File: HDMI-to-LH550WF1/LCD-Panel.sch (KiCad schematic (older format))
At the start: 15 parts

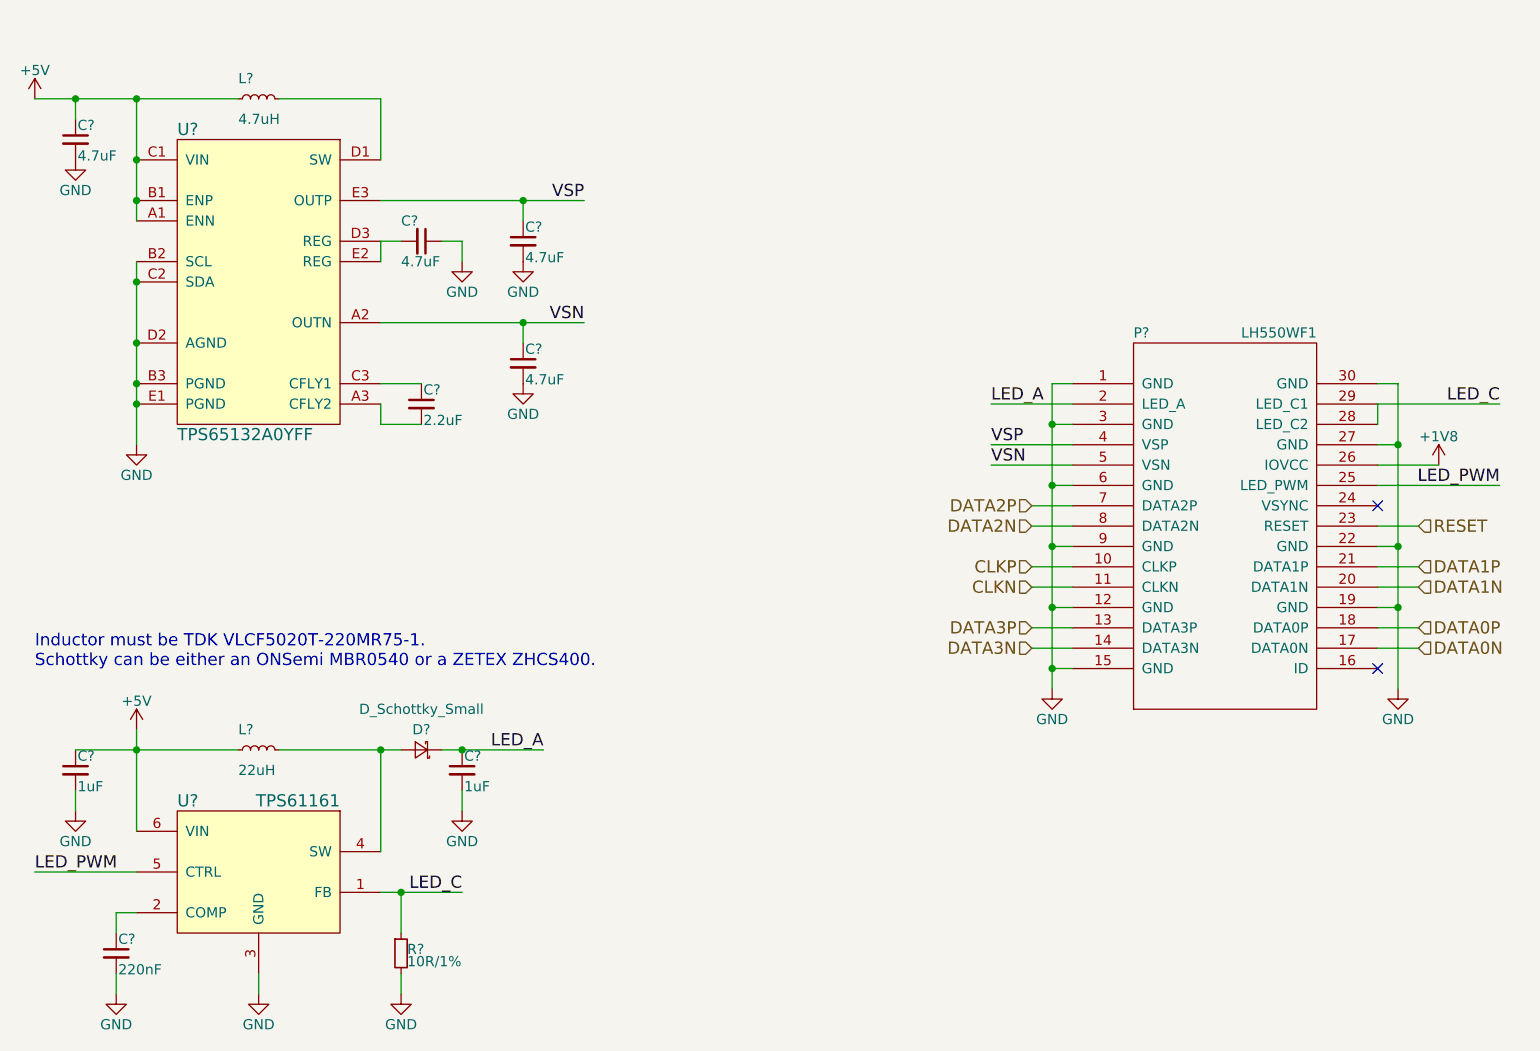
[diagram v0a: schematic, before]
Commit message: Annotated schematic and associated footprints
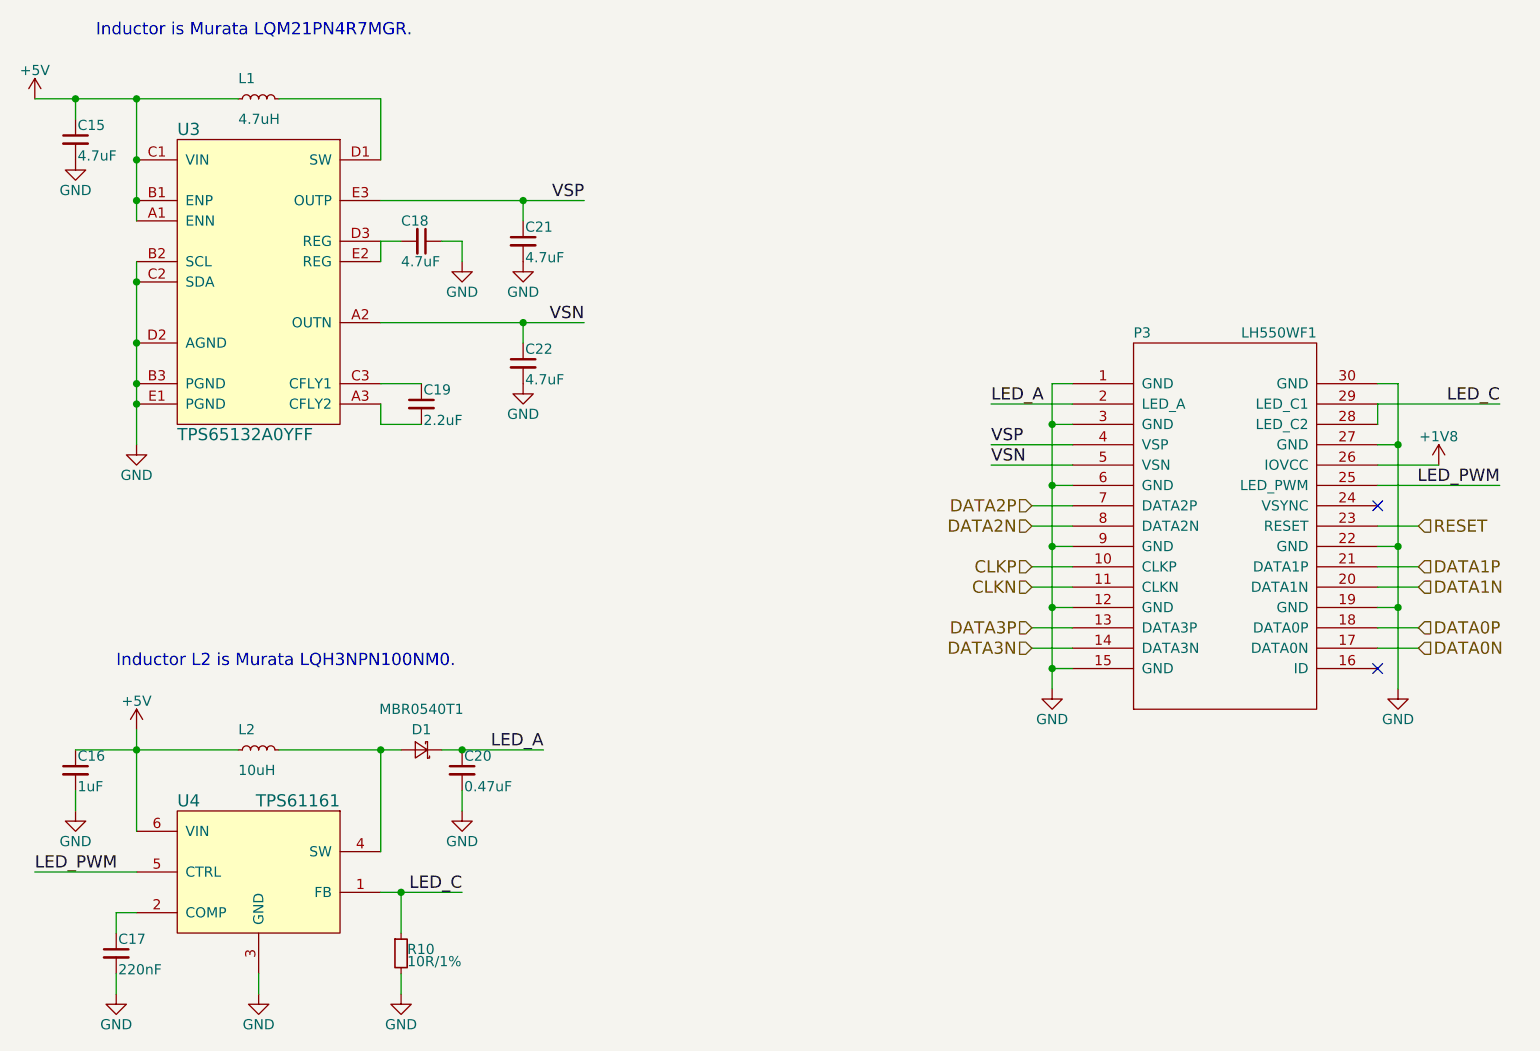
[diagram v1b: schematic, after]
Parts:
- C15, C16, C18, C19, C21, C22: renamed from C?; footprint (none) -> Capacitors_SMD:C_0603
- C17: renamed from C?; footprint (none) -> Capacitors_SMD:C_0402
- C20: renamed from C?; value 1uF -> 0.47uF; footprint (none) -> Capacitors_SMD:C_0603
- D1: renamed from D?; value D_Schottky_Small -> MBR0540T1; footprint (none) -> Diodes_SMD:SOD-123
- L1: renamed from L?; footprint (none) -> Resistors_SMD:R_0805
- L2: renamed from L?; value 22uH -> 10uH; footprint (none) -> Inductors:Inductor_Taiyo-Yuden_MD-3030
- P3: renamed from P?; footprint GB042-30S -> connectors:GB042-30S
- R10: renamed from R?; footprint (none) -> Resistors_SMD:R_0402
- U3: renamed from U?; footprint (none) -> miscellaneous:DSBGA-15_1.5x2.1mm_Pitch0.4mm
- U4: renamed from U?; footprint (none) -> miscellaneous:WSON-6_2x2mm_Pitch0.65mm
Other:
- note added: "Inductor L2 is Murata LQH3NPN100NM0."
- note added: "Inductor is Murata LQM21PN4R7MGR."
- note removed: "Inductor must be TDK VLCF5020T-220MR75-1.\nSchottky can be either an ONSemi MBR0540 or a ZETEX ZHCS400."
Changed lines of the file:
@@
 $EndDescr
 $Comp
-L LH550WF1 P?
+L LH550WF1 P3
 U 1 1 583923EB
 P 7950 3500
-F 0 "P?" H 7500 4450 50  0000 L CNN
+F 0 "P3" H 7500 4450 50  0000 L CNN
 F 1 "LH550WF1" H 8400 4450 50  0000 R CNN
-F 2 "GB042-30S" H 7500 2550 50  0001 L CNN
+F 2 "connectors:GB042-30S" H 7500 2550 50  0001 L CNN
 F 3 "" H 7800 2450 50  0001 C CNN
 	1    7950 3500
@@
 RESET
 $Comp
-L GND #PWR020
+L GND #PWR028
 U 1 1 58392710
 P 8800 4300
-F 0 "#PWR020" H 8800 4050 50  0001 C CNN
+F 0 "#PWR028" H 8800 4050 50  0001 C CNN
 F 1 "GND" H 8800 4150 50  0000 C CNN
 F 2 "" H 8800 4300 50  0000 C CNN
@@
 $EndComp
 $Comp
-L GND #PWR021
+L GND #PWR029
 U 1 1 58392726
 P 7100 4300
-F 0 "#PWR021" H 7100 4050 50  0001 C CNN
+F 0 "#PWR029" H 7100 4050 50  0001 C CNN
 F 1 "GND" H 7100 4150 50  0000 C CNN
 F 2 "" H 7100 4300 50  0000 C CNN
@@
 NoConn ~ 8700 4200
 $Comp
-L +1V8 #PWR022
+L +1V8 #PWR030
 U 1 1 58393DDA
 P 9000 3200
-F 0 "#PWR022" H 9000 3050 50  0001 C CNN
+F 0 "#PWR030" H 9000 3050 50  0001 C CNN
 F 1 "+1V8" H 9000 3340 50  0000 C CNN
 F 2 "" H 9000 3200 50  0000 C CNN
@@
 VSN
 $Comp
-L TPS65132xxYFF U?
+L TPS65132xxYFF U3
 U 1 1 583941C9
 P 3200 2300
-F 0 "U?" H 2800 3050 60  0000 L CNN
+F 0 "U3" H 2800 3050 60  0000 L CNN
 F 1 "TPS65132A0YFF" H 2800 1550 60  0000 L CNN
-F 2 "" H 3100 2700 60  0001 C CNN
+F 2 "miscellaneous:DSBGA-15_1.5x2.1mm_Pitch0.4mm" H 3100 2700 60  0001 C CNN
 F 3 "" H 3100 2700 60  0001 C CNN
 	1    3200 2300
@@
 $EndComp
 $Comp
-L TPS6116x U?
+L TPS6116x U4
 U 1 1 583944F1
 P 3200 5200
-F 0 "U?" H 2800 5550 60  0000 L CNN
+F 0 "U4" H 2800 5550 60  0000 L CNN
 F 1 "TPS61161" H 3600 5550 60  0000 R CNN
-F 2 "" H 3100 5200 60  0001 C CNN
+F 2 "miscellaneous:WSON-6_2x2mm_Pitch0.65mm" H 3100 5200 60  0001 C CNN
 F 3 "" H 3100 5200 60  0001 C CNN
 	1    3200 5200
@@
 LED_PWM
 $Comp
-L +5V #PWR023
+L +5V #PWR031
 U 1 1 58394FDE
 P 2600 4500
-F 0 "#PWR023" H 2600 4350 50  0001 C CNN
+F 0 "#PWR031" H 2600 4350 50  0001 C CNN
 F 1 "+5V" H 2600 4640 50  0000 C CNN
 F 2 "" H 2600 4500 50  0000 C CNN
@@
 $EndComp
 $Comp
-L C_Small C?
+L C_Small C16
 U 1 1 58395057
 P 2300 4700
-F 0 "C?" H 2310 4770 50  0000 L CNN
+F 0 "C16" H 2310 4770 50  0000 L CNN
 F 1 "1uF" H 2310 4620 50  0000 L CNN
-F 2 "" H 2300 4700 50  0000 C CNN
+F 2 "Capacitors_SMD:C_0603" H 2300 4700 50  0001 C CNN
 F 3 "" H 2300 4700 50  0000 C CNN
 	1    2300 4700
@@
 $EndComp
 $Comp
-L L_Small L?
+L L_Small L2
 U 1 1 58395114
 P 3200 4600
-F 0 "L?" V 3300 4700 50  0000 R CNN
-F 1 "22uH" V 3100 4700 50  0000 R CNN
-F 2 "" H 3200 4600 50  0000 C CNN
+F 0 "L2" V 3300 4700 50  0000 R CNN
+F 1 "10uH" V 3100 4700 50  0000 R CNN
+F 2 "Inductors:Inductor_Taiyo-Yuden_MD-3030" H 3200 4600 50  0001 C CNN
 F 3 "" H 3200 4600 50  0000 C CNN
 	1    3200 4600
@@
 $EndComp
 $Comp
-L GND #PWR024
+L GND #PWR032
 U 1 1 58395360
 P 2300 4900
-F 0 "#PWR024" H 2300 4650 50  0001 C CNN
+F 0 "#PWR032" H 2300 4650 50  0001 C CNN
 F 1 "GND" H 2300 4750 50  0000 C CNN
 F 2 "" H 2300 4900 50  0000 C CNN
@@
 $EndComp
 $Comp
-L C_Small C?
+L C_Small C17
 U 1 1 583959D0
 P 2500 5600
-F 0 "C?" H 2510 5670 50  0000 L CNN
+F 0 "C17" H 2510 5670 50  0000 L CNN
 F 1 "220nF" H 2510 5520 50  0000 L CNN
-F 2 "" H 2500 5600 50  0000 C CNN
+F 2 "Capacitors_SMD:C_0402" H 2500 5600 50  0001 C CNN
 F 3 "" H 2500 5600 50  0000 C CNN
 	1    2500 5600
@@
 $EndComp
 $Comp
-L GND #PWR025
+L GND #PWR033
 U 1 1 58395A08
 P 2500 5800
-F 0 "#PWR025" H 2500 5550 50  0001 C CNN
+F 0 "#PWR033" H 2500 5550 50  0001 C CNN
 F 1 "GND" H 2500 5650 50  0000 C CNN
 F 2 "" H 2500 5800 50  0000 C CNN
@@
 $EndComp
 $Comp
-L GND #PWR026
+L GND #PWR034
 U 1 1 58395A97
 P 3200 5800
-F 0 "#PWR026" H 3200 5550 50  0001 C CNN
+F 0 "#PWR034" H 3200 5550 50  0001 C CNN
 F 1 "GND" H 3200 5650 50  0000 C CNN
 F 2 "" H 3200 5800 50  0000 C CNN
@@
 $EndComp
 $Comp
-L GND #PWR027
+L GND #PWR035
 U 1 1 58395AB4
 P 3900 5800
-F 0 "#PWR027" H 3900 5550 50  0001 C CNN
+F 0 "#PWR035" H 3900 5550 50  0001 C CNN
 F 1 "GND" H 3900 5650 50  0000 C CNN
 F 2 "" H 3900 5800 50  0000 C CNN
@@
 $EndComp
 $Comp
-L C_Small C?
+L C_Small C20
 U 1 1 58395AE8
 P 4200 4700
-F 0 "C?" H 4210 4770 50  0000 L CNN
-F 1 "1uF" H 4210 4620 50  0000 L CNN
-F 2 "" H 4200 4700 50  0000 C CNN
+F 0 "C20" H 4210 4770 50  0000 L CNN
+F 1 "0.47uF" H 4210 4620 50  0000 L CNN
+F 2 "Capacitors_SMD:C_0603" H 4200 4700 50  0001 C CNN
 F 3 "" H 4200 4700 50  0000 C CNN
 	1    4200 4700
@@
 Connection ~ 3800 4600
 $Comp
-L D_Schottky_Small D?
+L D_Schottky_Small D1
 U 1 1 583961F5
 P 4000 4600
-F 0 "D?" H 4000 4500 50  0000 C CNN
-F 1 "D_Schottky_Small" H 4000 4400 50  0000 C CNN
-F 2 "" V 4000 4600 50  0000 C CNN
+F 0 "D1" H 4000 4500 50  0000 C CNN
+F 1 "MBR0540T1" H 4000 4400 50  0000 C CNN
+F 2 "Diodes_SMD:SOD-123" V 4000 4600 50  0001 C CNN
 F 3 "" V 4000 4600 50  0000 C CNN
 	1    4000 4600
@@
 	4100 4600 4600 4600
 $Comp
-L GND #PWR028
+L GND #PWR036
 U 1 1 583963D4
 P 4200 4900
-F 0 "#PWR028" H 4200 4650 50  0001 C CNN
+F 0 "#PWR036" H 4200 4650 50  0001 C CNN
 F 1 "GND" H 4200 4750 50  0000 C CNN
 F 2 "" H 4200 4900 50  0000 C CNN
@@
 	4200 4900 4200 4800
 $Comp
-L R_Small R?
+L R_Small R10
 U 1 1 58396477
 P 3900 5600
-F 0 "R?" H 3930 5620 50  0000 L CNN
+F 0 "R10" H 3930 5620 50  0000 L CNN
 F 1 "10R/1%" H 3930 5560 50  0000 L CNN
-F 2 "" H 3900 5600 50  0000 C CNN
+F 2 "Resistors_SMD:R_0402" H 3900 5600 50  0001 C CNN
 F 3 "" H 3900 5600 50  0000 C CNN
 	1    3900 5600
@@
 Connection ~ 4200 4600
 Connection ~ 3900 5300
-Text Notes 2100 4200 0    60   ~ 0
-Inductor must be TDK VLCF5020T-220MR75-1.\nSchottky can be either an ONSemi MBR0540 or a ZETEX ZHCS400.
-$Comp
-L +5V #PWR029
+Text Notes 2500 4200 0    60   ~ 0
+Inductor L2 is Murata LQH3NPN100NM0.
+$Comp
+L +5V #PWR037
 U 1 1 58397D18
 P 2100 1400
-F 0 "#PWR029" H 2100 1250 50  0001 C CNN
+F 0 "#PWR037" H 2100 1250 50  0001 C CNN
 F 1 "+5V" H 2100 1540 50  0000 C CNN
 F 2 "" H 2100 1400 50  0000 C CNN
@@
 $EndComp
 $Comp
-L L_Small L?
+L L_Small L1
 U 1 1 58397E29
 P 3200 1400
-F 0 "L?" V 3300 1500 50  0000 R CNN
+F 0 "L1" V 3300 1500 50  0000 R CNN
 F 1 "4.7uH" V 3100 1500 50  0000 R CNN
-F 2 "" H 3200 1400 50  0000 C CNN
+F 2 "Resistors_SMD:R_0805" H 3200 1400 50  0001 C CNN
 F 3 "" H 3200 1400 50  0000 C CNN
 	1    3200 1400
@@
 	2100 1400 3100 1400
 $Comp
-L C_Small C?
+L C_Small C15
 U 1 1 58398042
 P 2300 1600
-F 0 "C?" H 2310 1670 50  0000 L CNN
+F 0 "C15" H 2310 1670 50  0000 L CNN
 F 1 "4.7uF" H 2310 1520 50  0000 L CNN
-F 2 "" H 2300 1600 50  0000 C CNN
+F 2 "Capacitors_SMD:C_0603" H 2300 1600 50  0001 C CNN
 F 3 "" H 2300 1600 50  0000 C CNN
 	1    2300 1600
@@
 Connection ~ 2300 1400
 $Comp
-L GND #PWR030
+L GND #PWR038
 U 1 1 583981F9
 P 2300 1700
-F 0 "#PWR030" H 2300 1450 50  0001 C CNN
+F 0 "#PWR038" H 2300 1450 50  0001 C CNN
 F 1 "GND" H 2300 1550 50  0000 C CNN
 F 2 "" H 2300 1700 50  0000 C CNN
@@
 Connection ~ 2600 2900
 $Comp
-L GND #PWR031
+L GND #PWR039
 U 1 1 583983E8
 P 2600 3100
-F 0 "#PWR031" H 2600 2850 50  0001 C CNN
+F 0 "#PWR039" H 2600 2850 50  0001 C CNN
 F 1 "GND" H 2600 2950 50  0000 C CNN
 F 2 "" H 2600 3100 50  0000 C CNN
@@
 	3800 3000 3800 2900
 $Comp
-L C_Small C?
+L C_Small C19
 U 1 1 583986B8
 P 4000 2900
-F 0 "C?" H 4010 2970 50  0000 L CNN
+F 0 "C19" H 4010 2970 50  0000 L CNN
 F 1 "2.2uF" H 4010 2820 50  0000 L CNN
-F 2 "" H 4000 2900 50  0000 C CNN
+F 2 "Capacitors_SMD:C_0603" H 4000 2900 50  0001 C CNN
 F 3 "" H 4000 2900 50  0000 C CNN
 	1    4000 2900
@@
 	3800 2200 3800 2100
 $Comp
-L C_Small C?
+L C_Small C18
 U 1 1 58398AB8
 P 4000 2100
-F 0 "C?" V 3900 2000 50  0000 L CNN
+F 0 "C18" V 3900 2000 50  0000 L CNN
 F 1 "4.7uF" V 4100 2000 50  0000 L CNN
-F 2 "" H 4000 2100 50  0000 C CNN
+F 2 "Capacitors_SMD:C_0603" H 4000 2100 50  0001 C CNN
 F 3 "" H 4000 2100 50  0000 C CNN
 	1    4000 2100
@@
 	4200 2100 4200 2200
 $Comp
-L GND #PWR032
+L GND #PWR040
 U 1 1 58398C7D
 P 4200 2200
-F 0 "#PWR032" H 4200 1950 50  0001 C CNN
+F 0 "#PWR040" H 4200 1950 50  0001 C CNN
 F 1 "GND" H 4200 2050 50  0000 C CNN
 F 2 "" H 4200 2200 50  0000 C CNN
@@
 $EndComp
 $Comp
-L C_Small C?
+L C_Small C21
 U 1 1 58398CAF
 P 4500 2100
-F 0 "C?" H 4510 2170 50  0000 L CNN
+F 0 "C21" H 4510 2170 50  0000 L CNN
 F 1 "4.7uF" H 4510 2020 50  0000 L CNN
-F 2 "" H 4500 2100 50  0000 C CNN
+F 2 "Capacitors_SMD:C_0603" H 4500 2100 50  0001 C CNN
 F 3 "" H 4500 2100 50  0000 C CNN
 	1    4500 2100
@@
 Connection ~ 4500 1900
 $Comp
-L GND #PWR033
+L GND #PWR041
 U 1 1 58398F9F
 P 4500 2200
-F 0 "#PWR033" H 4500 1950 50  0001 C CNN
+F 0 "#PWR041" H 4500 1950 50  0001 C CNN
 F 1 "GND" H 4500 2050 50  0000 C CNN
 F 2 "" H 4500 2200 50  0000 C CNN
@@
 $EndComp
 $Comp
-L C_Small C?
+L C_Small C22
 U 1 1 58398FD4
 P 4500 2700
-F 0 "C?" H 4510 2770 50  0000 L CNN
+F 0 "C22" H 4510 2770 50  0000 L CNN
 F 1 "4.7uF" H 4510 2620 50  0000 L CNN
-F 2 "" H 4500 2700 50  0000 C CNN
+F 2 "Capacitors_SMD:C_0603" H 4500 2700 50  0001 C CNN
 F 3 "" H 4500 2700 50  0000 C CNN
 	1    4500 2700
@@
 $EndComp
 $Comp
-L GND #PWR034
+L GND #PWR042
 U 1 1 58399019
 P 4500 2800
-F 0 "#PWR034" H 4500 2550 50  0001 C CNN
+F 0 "#PWR042" H 4500 2550 50  0001 C CNN
 F 1 "GND" H 4500 2650 50  0000 C CNN
 F 2 "" H 4500 2800 50  0000 C CNN
@@
 Connection ~ 2600 2600
 Connection ~ 2600 2300
+Text Notes 2400 1100 0    60   ~ 0
+Inductor is Murata LQM21PN4R7MGR.
 $EndSCHEMATC

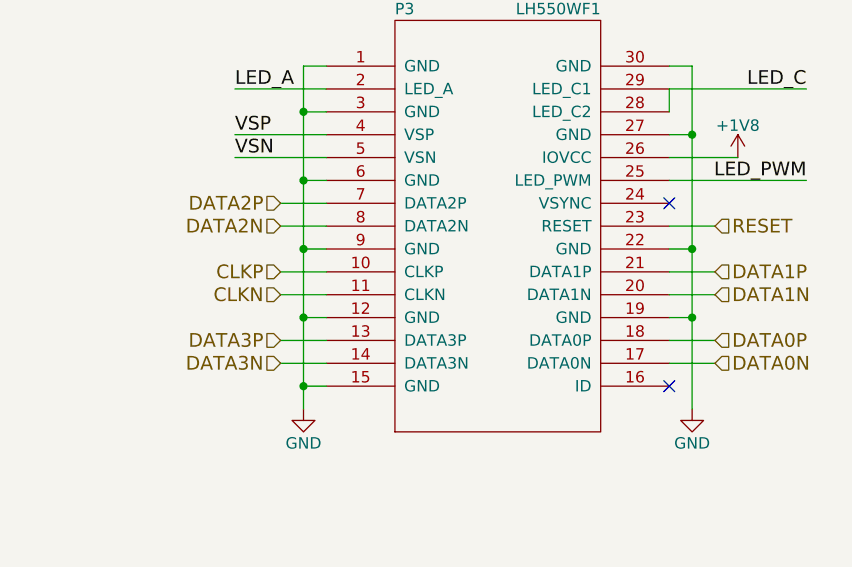
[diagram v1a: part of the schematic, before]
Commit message: Renamed some nets to enable differential routing
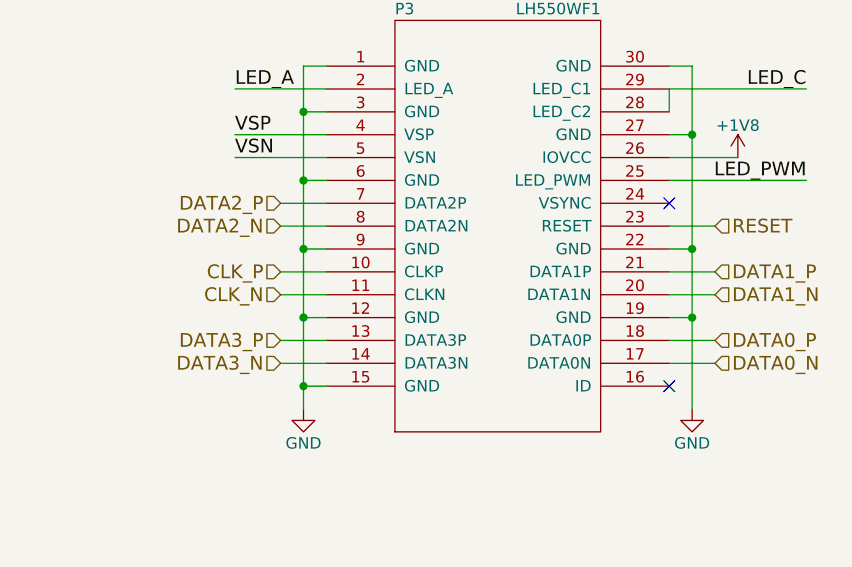
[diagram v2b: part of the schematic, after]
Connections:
- net CLKN renamed CLK_N
- net CLKP renamed CLK_P
- net DATA0N renamed DATA0_N
- net DATA0P renamed DATA0_P
- net DATA1N renamed DATA1_N
- net DATA1P renamed DATA1_P
- net DATA2N renamed DATA2_N
- net DATA2P renamed DATA2_P
- net DATA3N renamed DATA3_N
- net DATA3P renamed DATA3_P
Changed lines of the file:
@@
 $EndComp
 Text HLabel 7000 4000 0    60   Input ~ 0
-DATA3P
+DATA3_P
 Text HLabel 7000 4100 0    60   Input ~ 0
-DATA3N
+DATA3_N
 Text HLabel 7000 3400 0    60   Input ~ 0
-DATA2P
+DATA2_P
 Text HLabel 7000 3500 0    60   Input ~ 0
-DATA2N
+DATA2_N
 Text HLabel 7000 3700 0    60   Input ~ 0
-CLKP
+CLK_P
 Text HLabel 7000 3800 0    60   Input ~ 0
-CLKN
+CLK_N
 Text HLabel 8900 3800 2    60   Input ~ 0
-DATA1N
+DATA1_N
 Text HLabel 8900 3700 2    60   Input ~ 0
-DATA1P
+DATA1_P
 Text HLabel 8900 4000 2    60   Input ~ 0
-DATA0P
+DATA0_P
 Text HLabel 8900 4100 2    60   Input ~ 0
-DATA0N
+DATA0_N
 Text HLabel 8900 3500 2    60   Input ~ 0
 RESET
